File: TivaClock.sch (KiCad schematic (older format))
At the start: 6 parts

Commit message: add some more stuff
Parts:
- gave numbers to parts that had none: 4
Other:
- moved on the sheet: J2, J4, J?
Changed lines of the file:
@@
 $EndDescr
 $Comp
-L Conn_01x10 J?
+L Conn_01x10 J1
 U 1 1 5A5BEAC9
 P 2800 2300
-F 0 "J?" H 2800 2800 50  0000 C CNN
+F 0 "J1" H 2800 2800 50  0000 C CNN
 F 1 "Conn_01x10" H 2800 1700 50  0000 C CNN
 F 2 "" H 2800 2300 50  0001 C CNN
@@
 $EndComp
 $Comp
-L Conn_01x10 J?
+L Conn_01x10 J3
 U 1 1 5A5BEB8A
 P 3350 2300
-F 0 "J?" H 3350 2800 50  0000 C CNN
+F 0 "J3" H 3350 2800 50  0000 C CNN
 F 1 "Conn_01x10" H 3350 1700 50  0000 C CNN
 F 2 "" H 3350 2300 50  0001 C CNN
@@
 $EndComp
 $Comp
-L Conn_01x10 J?
+L Conn_01x10 J4
 U 1 1 5A5BED0F
-P 5600 2250
-F 0 "J?" H 5600 2750 50  0000 C CNN
-F 1 "Conn_01x10" H 5600 1650 50  0000 C CNN
-F 2 "" H 5600 2250 50  0001 C CNN
-F 3 "" H 5600 2250 50  0001 C CNN
-	1    5600 2250
+P 7800 2300
+F 0 "J4" H 7800 2800 50  0000 C CNN
+F 1 "Conn_01x10" H 7800 1700 50  0000 C CNN
+F 2 "" H 7800 2300 50  0001 C CNN
+F 3 "" H 7800 2300 50  0001 C CNN
+	1    7800 2300
 	1    0    0    -1
 $EndComp
 $Comp
-L Conn_01x10 J?
+L Conn_01x10 J2
 U 1 1 5A5BED3B
-P 6300 2300
-F 0 "J?" H 6300 2800 50  0000 C CNN
-F 1 "Conn_01x10" H 6300 1700 50  0000 C CNN
-F 2 "" H 6300 2300 50  0001 C CNN
-F 3 "" H 6300 2300 50  0001 C CNN
-	1    6300 2300
+P 8500 2300
+F 0 "J2" H 8500 2800 50  0000 C CNN
+F 1 "Conn_01x10" H 8500 1700 50  0000 C CNN
+F 2 "" H 8500 2300 50  0001 C CNN
+F 3 "" H 8500 2300 50  0001 C CNN
+	1    8500 2300
 	-1   0    0    -1
 $EndComp
@@
 L Conn_01x20 J?
 U 1 1 5A5BED71
-P 8200 4600
-F 0 "J?" H 8200 5600 50  0000 C CNN
-F 1 "Conn_01x20" H 8200 3500 50  0000 C CNN
-F 2 "" H 8200 4600 50  0001 C CNN
-F 3 "" H 8200 4600 50  0001 C CNN
-	1    8200 4600
+P 5200 4550
+F 0 "J?" H 5200 5550 50  0000 C CNN
+F 1 "Conn_01x20" H 5200 3450 50  0000 C CNN
+F 2 "" H 5200 4550 50  0001 C CNN
+F 3 "" H 5200 4550 50  0001 C CNN
+	1    5200 4550
 	1    0    0    -1
 $EndComp
@@
 L Conn_01x20 J?
 U 1 1 5A5BEDA4
-P 8950 4700
-F 0 "J?" H 8950 5700 50  0000 C CNN
-F 1 "Conn_01x20" H 8950 3600 50  0000 C CNN
-F 2 "" H 8950 4700 50  0001 C CNN
-F 3 "" H 8950 4700 50  0001 C CNN
-	1    8950 4700
+P 5950 4650
+F 0 "J?" H 5950 5650 50  0000 C CNN
+F 1 "Conn_01x20" H 5950 3550 50  0000 C CNN
+F 2 "" H 5950 4650 50  0001 C CNN
+F 3 "" H 5950 4650 50  0001 C CNN
+	1    5950 4650
 	-1   0    0    1
 $EndComp
-Text Label 7550 3700 0    60   ~ 0
+Text Label 4550 3650 0    60   ~ 0
 DS18B20
-Text Label 7550 3800 0    60   ~ 0
+Text Label 4550 3750 0    60   ~ 0
 1302RST
-Text Label 7550 3900 0    60   ~ 0
+Text Label 4550 3850 0    60   ~ 0
 1302IO
-Text Label 7550 4000 0    60   ~ 0
+Text Label 4550 3950 0    60   ~ 0
 1302CLK
-Text Label 7550 4100 0    60   ~ 0
+Text Label 4550 4050 0    60   ~ 0
 BEEP
-Text Label 7550 4500 0    60   ~ 0
+Text Label 4550 4450 0    60   ~ 0
 RESET
-Text Label 7550 4600 0    60   ~ 0
+Text Label 4550 4550 0    60   ~ 0
 RXD
-Text Label 7550 4700 0    60   ~ 0
+Text Label 4550 4650 0    60   ~ 0
 TXD
-Text Label 7550 4800 0    60   ~ 0
+Text Label 4550 4750 0    60   ~ 0
 MODE
-Text Label 7550 4900 0    60   ~ 0
+Text Label 4550 4850 0    60   ~ 0
 PLUS
-Text Label 7550 5000 0    60   ~ 0
+Text Label 4550 4950 0    60   ~ 0
 Bit8
-Text Label 7550 5100 0    60   ~ 0
+Text Label 4550 5050 0    60   ~ 0
 Bit9
-Text Label 7550 5200 0    60   ~ 0
+Text Label 4550 5150 0    60   ~ 0
 Bit10
-Text Label 7550 5300 0    60   ~ 0
+Text Label 4550 5250 0    60   ~ 0
 Bit11
-Text Label 7550 5600 0    60   ~ 0
+Text Label 4550 5550 0    60   ~ 0
 GND
-Text Label 9300 5600 0    60   ~ 0
+Text Label 6300 5550 0    60   ~ 0
 Bit0
-Text Label 9300 5500 0    60   ~ 0
+Text Label 6300 5450 0    60   ~ 0
 Bit1
-Text Label 9300 5400 0    60   ~ 0
+Text Label 6300 5350 0    60   ~ 0
 Bit2
-Text Label 9300 5300 0    60   ~ 0
+Text Label 6300 5250 0    60   ~ 0
 Bit3
-Text Label 9300 5200 0    60   ~ 0
+Text Label 6300 5150 0    60   ~ 0
 Bit4
-Text Label 9300 5100 0    60   ~ 0
+Text Label 6300 5050 0    60   ~ 0
 Bit5
-Text Label 9300 5000 0    60   ~ 0
+Text Label 6300 4950 0    60   ~ 0
 Bit6
-Text Label 9300 4900 0    60   ~ 0
+Text Label 6300 4850 0    60   ~ 0
 Bit7
-Text Label 9300 4600 0    60   ~ 0
+Text Label 6300 4550 0    60   ~ 0
 VCC
-Text Label 9300 4500 0    60   ~ 0
+Text Label 6300 4450 0    60   ~ 0
 X7
-Text Label 9300 4400 0    60   ~ 0
+Text Label 6300 4350 0    60   ~ 0
 X6
-Text Label 9300 4300 0    60   ~ 0
+Text Label 6300 4250 0    60   ~ 0
 X5
-Text Label 9300 4200 0    60   ~ 0
+Text Label 6300 4150 0    60   ~ 0
 X4
-Text Label 9300 4100 0    60   ~ 0
+Text Label 6300 4050 0    60   ~ 0
 X3
-Text Label 9300 4000 0    60   ~ 0
+Text Label 6300 3950 0    60   ~ 0
 X2
-Text Label 9300 3900 0    60   ~ 0
+Text Label 6300 3850 0    60   ~ 0
 X1
-Text Label 9300 3800 0    60   ~ 0
+Text Label 6300 3750 0    60   ~ 0
 X0
-Text Label 9300 3700 0    60   ~ 0
+Text Label 6300 3650 0    60   ~ 0
 VCC
 $EndSCHEMATC

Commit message: connect important peripherals
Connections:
- net BEEP: now also J2.2 (Pin_2), J?.5 (Pin_5)
- net GND: now also J2.1 (Pin_1), J3.2 (Pin_2), J?.20 (Pin_20)
- net RESET: now also J2.5 (Pin_5), J?.9 (Pin_9)
- net RXD: now also J1.3 (Pin_3), J?.10 (Pin_10)
- net TXD: now also J1.4 (Pin_4), J?.11 (Pin_11)
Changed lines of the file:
@@
 LIBS:contrib
 LIBS:valves
+LIBS:TivaClock-cache
 EELAYER 25 0
 EELAYER END
@@
 Text Label 6300 3650 0    60   ~ 0
 VCC
+Wire Wire Line
+	5000 4050 4350 4050
+Wire Wire Line
+	4350 4050 4350 3350
+Wire Wire Line
+	4350 3350 9000 3350
+Wire Wire Line
+	9000 3350 9000 2000
+Wire Wire Line
+	9000 2000 8700 2000
+Wire Wire Line
+	8700 2300 8900 2300
+Wire Wire Line
+	8900 2300 8900 3200
+Wire Wire Line
+	8900 3200 4200 3200
+Wire Wire Line
+	4200 3200 4200 4450
+Wire Wire Line
+	4200 4450 5000 4450
+Wire Wire Line
+	5000 4550 2150 4550
+Wire Wire Line
+	2150 4550 2150 2100
+Wire Wire Line
+	2150 2100 2600 2100
+Wire Wire Line
+	5000 4650 2300 4650
+Wire Wire Line
+	2300 4650 2300 2200
+Wire Wire Line
+	2300 2200 2600 2200
+Wire Wire Line
+	3550 2000 7000 2000
+Wire Wire Line
+	7000 2000 7000 1700
+Wire Wire Line
+	7000 1700 8800 1700
+Wire Wire Line
+	8800 1700 8800 1900
+Wire Wire Line
+	8800 1900 8700 1900
+Wire Wire Line
+	5000 5550 3900 5550
+Wire Wire Line
+	3900 5550 3900 2000
+Connection ~ 3900 2000
 $EndSCHEMATC

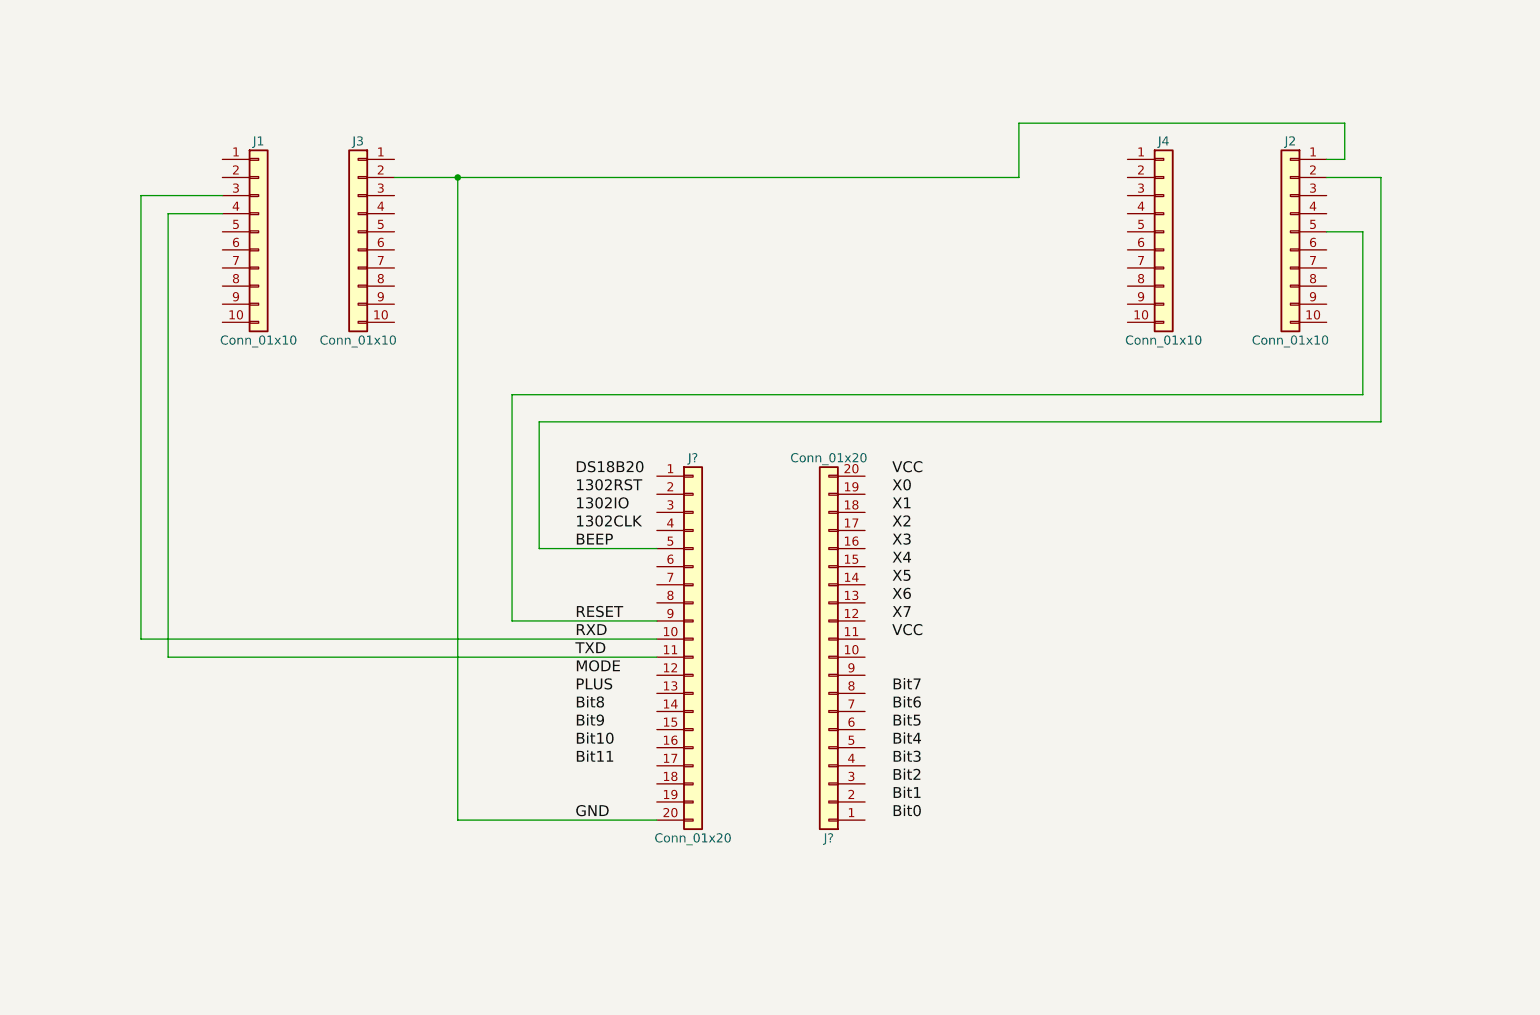
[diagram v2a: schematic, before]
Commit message: connected LED wires
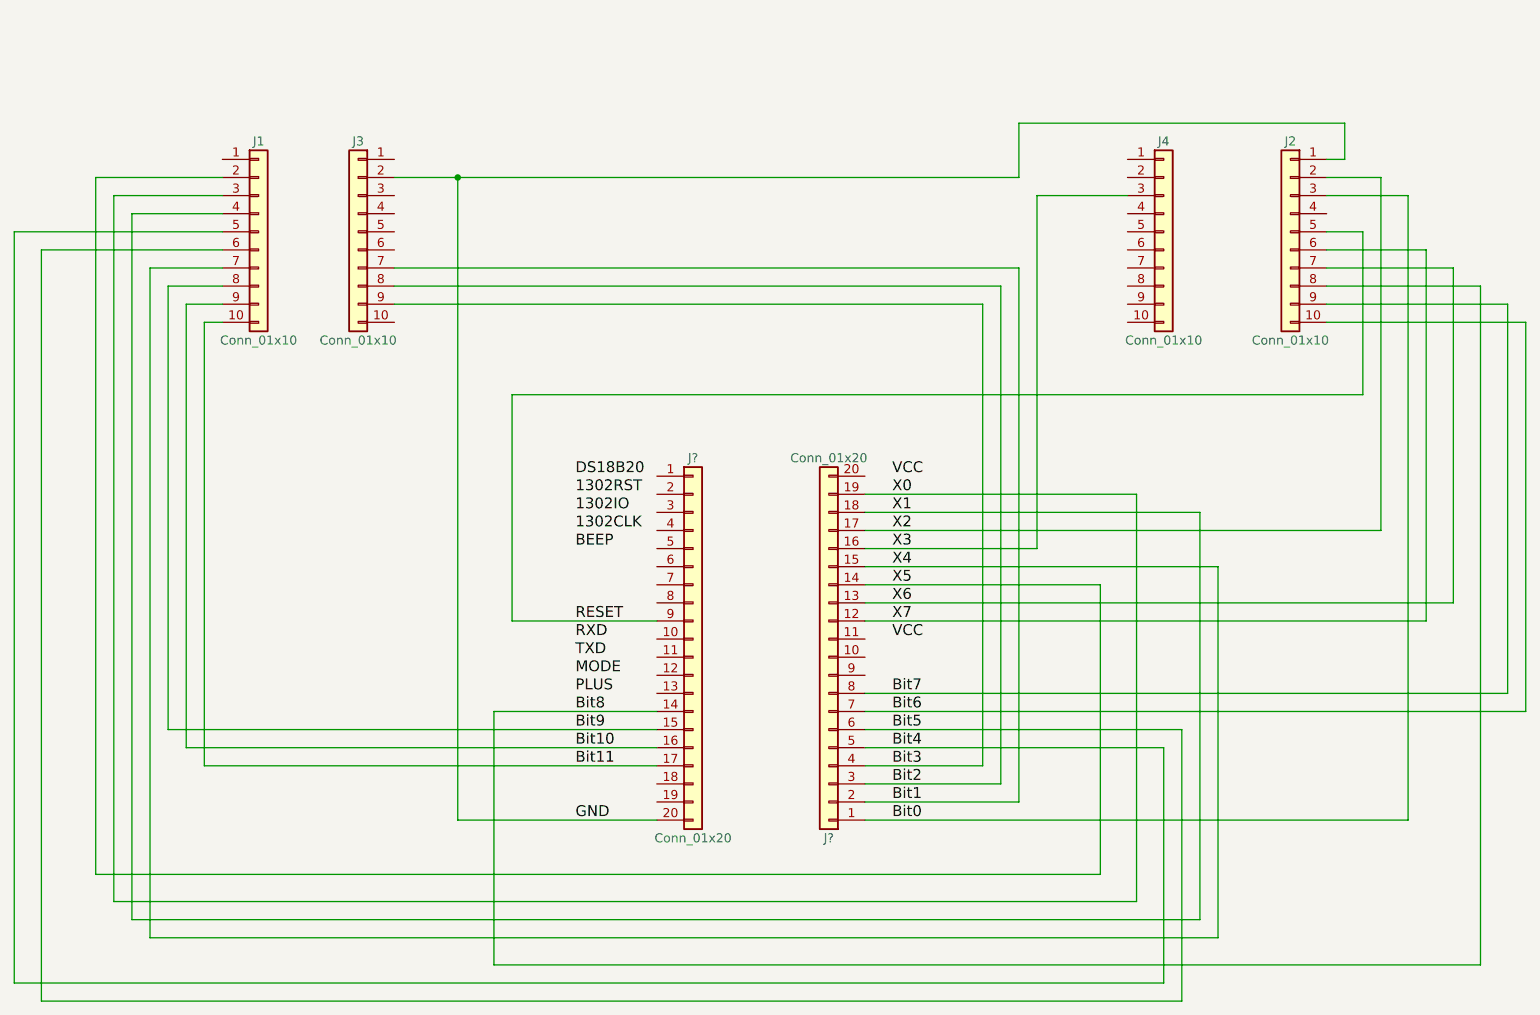
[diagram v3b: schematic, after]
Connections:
- net BEEP: no longer J2.2 (Pin_2), J?.5 (Pin_5)
- net Bit0: now also J2.3 (Pin_3), J?.1 (Pin_1)
- net Bit1: now also J3.7 (Pin_7), J?.2 (Pin_2)
- net Bit10: now also J1.9 (Pin_9), J?.16 (Pin_16)
- net Bit11: now also J1.10 (Pin_10), J?.17 (Pin_17)
- net Bit2: now also J3.8 (Pin_8), J?.3 (Pin_3)
- net Bit3: now also J3.9 (Pin_9), J?.4 (Pin_4)
- net Bit4: now also J1.5 (Pin_5), J?.5 (Pin_5)
- net Bit5: now also J1.6 (Pin_6), J?.6 (Pin_6)
- net Bit6: now also J2.10 (Pin_10), J?.7 (Pin_7)
- net Bit7: now also J2.9 (Pin_9), J?.8 (Pin_8)
- net Bit8: now also J2.8 (Pin_8), J?.14 (Pin_14)
- net Bit9: now also J1.8 (Pin_8), J?.15 (Pin_15)
- net RXD: no longer J1.3 (Pin_3), J?.10 (Pin_10)
- net TXD: no longer J1.4 (Pin_4), J?.11 (Pin_11)
- net X0: now also J1.3 (Pin_3), J?.19 (Pin_19)
- net X1: now also J1.4 (Pin_4), J?.18 (Pin_18)
- net X2: now also J2.2 (Pin_2), J?.17 (Pin_17)
- net X3: now also J4.3 (Pin_3), J?.16 (Pin_16)
- net X4: now also J1.7 (Pin_7), J?.15 (Pin_15)
- net X5: now also J1.2 (Pin_2), J?.14 (Pin_14)
- net X6: now also J2.7 (Pin_7), J?.13 (Pin_13)
- net X7: now also J2.6 (Pin_6), J?.12 (Pin_12)
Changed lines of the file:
@@
 VCC
-Wire Wire Line
-	5000 4050 4350 4050
-Wire Wire Line
-	4350 4050 4350 3350
-Wire Wire Line
-	4350 3350 9000 3350
-Wire Wire Line
-	9000 3350 9000 2000
-Wire Wire Line
-	9000 2000 8700 2000
 Wire Wire Line
 	8700 2300 8900 2300
@@
 	4200 4450 5000 4450
 Wire Wire Line
-	5000 4550 2150 4550
+	3550 2000 3900 2000
 Wire Wire Line
-	2150 4550 2150 2100
-Wire Wire Line
-	2150 2100 2600 2100
-Wire Wire Line
-	5000 4650 2300 4650
-Wire Wire Line
-	2300 4650 2300 2200
-Wire Wire Line
-	2300 2200 2600 2200
-Wire Wire Line
-	3550 2000 7000 2000
+	3900 2000 7000 2000
 Wire Wire Line
 	7000 2000 7000 1700
@@
 	3900 5550 3900 2000
 Connection ~ 3900 2000
+Wire Wire Line
+	2600 2000 1900 2000
+Wire Wire Line
+	1900 2000 1900 5850
+Wire Wire Line
+	1900 5850 7450 5850
+Wire Wire Line
+	7450 5850 7450 4250
+Wire Wire Line
+	7450 4250 6150 4250
+Wire Wire Line
+	2600 2100 2000 2100
+Wire Wire Line
+	2000 2100 2000 6000
+Wire Wire Line
+	2000 6000 7650 6000
+Wire Wire Line
+	7650 6000 7650 3750
+Wire Wire Line
+	7650 3750 6150 3750
+Wire Wire Line
+	2600 2200 2100 2200
+Wire Wire Line
+	2100 2200 2100 6100
+Wire Wire Line
+	2100 6100 8000 6100
+Wire Wire Line
+	8000 6100 8000 3850
+Wire Wire Line
+	8000 3850 6150 3850
+Wire Wire Line
+	2600 2500 2200 2500
+Wire Wire Line
+	2200 2500 2200 6200
+Wire Wire Line
+	2200 6200 8100 6200
+Wire Wire Line
+	8100 6200 8100 4150
+Wire Wire Line
+	8100 4150 6150 4150
+Wire Wire Line
+	2600 2600 2300 2600
+Wire Wire Line
+	2300 2600 2300 5050
+Wire Wire Line
+	2300 5050 5000 5050
+Wire Wire Line
+	2600 2700 2400 2700
+Wire Wire Line
+	2400 2700 2400 5150
+Wire Wire Line
+	2400 5150 5000 5150
+Wire Wire Line
+	2600 2800 2500 2800
+Wire Wire Line
+	2500 2800 2500 5250
+Wire Wire Line
+	2500 5250 5000 5250
+Wire Wire Line
+	8700 2000 9000 2000
+Wire Wire Line
+	9000 2000 9000 3950
+Wire Wire Line
+	9000 3950 6150 3950
+Wire Wire Line
+	8700 2100 9150 2100
+Wire Wire Line
+	9150 2100 9150 5550
+Wire Wire Line
+	9150 5550 6150 5550
+Wire Wire Line
+	8700 2400 9250 2400
+Wire Wire Line
+	9250 2400 9250 4450
+Wire Wire Line
+	9250 4450 6150 4450
+Wire Wire Line
+	8700 2500 9400 2500
+Wire Wire Line
+	9400 2500 9400 4350
+Wire Wire Line
+	9400 4350 6150 4350
+Wire Wire Line
+	8700 2600 9550 2600
+Wire Wire Line
+	9550 2600 9550 6350
+Wire Wire Line
+	9550 6350 4100 6350
+Wire Wire Line
+	4100 6350 4100 4950
+Wire Wire Line
+	4100 4950 5000 4950
+Wire Wire Line
+	8700 2700 9700 2700
+Wire Wire Line
+	9700 2700 9700 4850
+Wire Wire Line
+	9700 4850 6150 4850
+Wire Wire Line
+	8700 2800 9800 2800
+Wire Wire Line
+	9800 2800 9800 4950
+Wire Wire Line
+	9800 4950 6150 4950
+Wire Wire Line
+	3550 2500 7000 2500
+Wire Wire Line
+	7000 2500 7000 5450
+Wire Wire Line
+	7000 5450 6150 5450
+Wire Wire Line
+	3550 2600 6900 2600
+Wire Wire Line
+	6900 2600 6900 5350
+Wire Wire Line
+	6900 5350 6150 5350
+Wire Wire Line
+	3550 2700 6800 2700
+Wire Wire Line
+	6800 2700 6800 5250
+Wire Wire Line
+	6800 5250 6150 5250
+Wire Wire Line
+	7600 2100 7100 2100
+Wire Wire Line
+	7100 2100 7100 4050
+Wire Wire Line
+	7100 4050 6150 4050
+Wire Wire Line
+	2600 2300 1450 2300
+Wire Wire Line
+	1450 2300 1450 6450
+Wire Wire Line
+	1450 6450 7800 6450
+Wire Wire Line
+	7800 6450 7800 5150
+Wire Wire Line
+	7800 5150 6150 5150
+Wire Wire Line
+	2600 2400 1600 2400
+Wire Wire Line
+	1600 2400 1600 6550
+Wire Wire Line
+	1600 6550 7900 6550
+Wire Wire Line
+	7900 6550 7900 5050
+Wire Wire Line
+	7900 5050 6150 5050
 $EndSCHEMATC

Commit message: connected all remaining pins
except power
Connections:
- net 1302CLK: now also J4.5 (Pin_5), J?.4 (Pin_4)
- net 1302IO: now also J4.6 (Pin_6), J?.3 (Pin_3)
- net 1302RST: now also J4.7 (Pin_7), J?.2 (Pin_2)
- net BEEP: now also J4.4 (Pin_4), J?.5 (Pin_5)
- net DS18B20: now also J3.5 (Pin_5), J?.1 (Pin_1)
- net MODE: now also J4.10 (Pin_10), J?.12 (Pin_12)
- net PLUS: now also J2.4 (Pin_4), J?.13 (Pin_13)
- net RXD: now also J4.8 (Pin_8), J?.10 (Pin_10)
- net TXD: now also J4.9 (Pin_9), J?.11 (Pin_11)
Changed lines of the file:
@@
 	4200 4450 5000 4450
 Wire Wire Line
-	3550 2000 3900 2000
-Wire Wire Line
-	3900 2000 7000 2000
+	3550 2000 7000 2000
 Wire Wire Line
 	7000 2000 7000 1700
@@
 Wire Wire Line
 	7900 5050 6150 5050
+Wire Wire Line
+	7600 2200 4050 2200
+Wire Wire Line
+	4050 2200 4050 4050
+Wire Wire Line
+	4050 4050 5000 4050
+Wire Wire Line
+	7600 2800 3800 2800
+Wire Wire Line
+	3800 2800 3800 4750
+Wire Wire Line
+	3800 4750 5000 4750
+Wire Wire Line
+	8700 2200 8800 2200
+Wire Wire Line
+	8800 2200 8800 3400
+Wire Wire Line
+	8800 3400 3500 3400
+Wire Wire Line
+	3500 3400 3500 4850
+Wire Wire Line
+	3500 4850 5000 4850
+Wire Wire Line
+	7600 2300 4300 2300
+Wire Wire Line
+	4300 2300 4300 3950
+Wire Wire Line
+	4300 3950 5000 3950
+Wire Wire Line
+	4400 3850 5000 3850
+Wire Wire Line
+	4400 3850 4400 2400
+Wire Wire Line
+	4400 2400 7600 2400
+Wire Wire Line
+	7600 2500 7200 2500
+Wire Wire Line
+	7200 2500 7200 2950
+Wire Wire Line
+	7200 2950 4500 2950
+Wire Wire Line
+	4500 2950 4500 3750
+Wire Wire Line
+	4500 3750 5000 3750
+Wire Wire Line
+	3550 2300 3700 2300
+Wire Wire Line
+	3700 2300 3700 3650
+Wire Wire Line
+	3700 3650 5000 3650
+Wire Wire Line
+	7600 2600 7300 2600
+Wire Wire Line
+	7300 2600 7300 3050
+Wire Wire Line
+	7300 3050 3250 3050
+Wire Wire Line
+	3250 3050 3250 4550
+Wire Wire Line
+	3250 4550 5000 4550
+Wire Wire Line
+	7600 2700 7400 2700
+Wire Wire Line
+	7400 2700 7400 3100
+Wire Wire Line
+	7400 3100 3100 3100
+Wire Wire Line
+	3100 3100 3100 4650
+Wire Wire Line
+	3100 4650 5000 4650
 $EndSCHEMATC

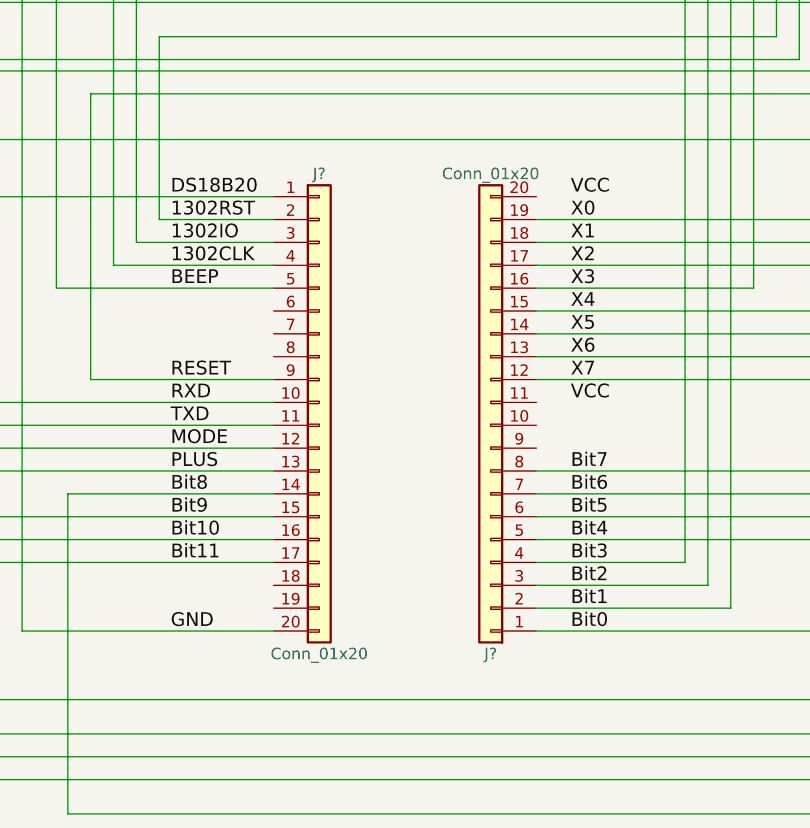
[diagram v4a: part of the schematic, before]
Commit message: annotate clock headers
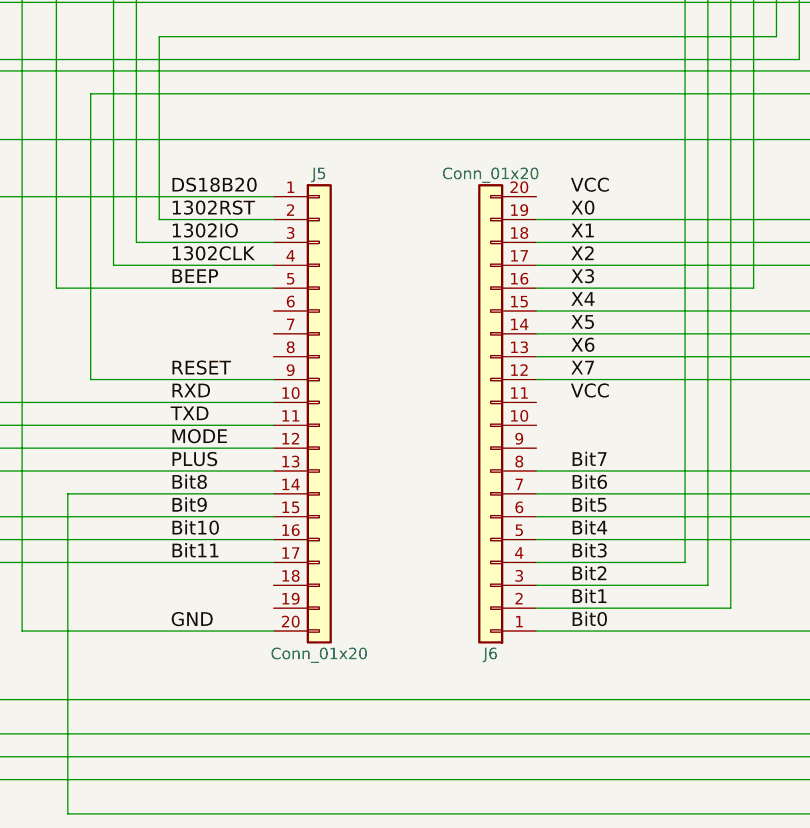
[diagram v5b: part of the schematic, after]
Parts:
- gave numbers to parts that had none: 2
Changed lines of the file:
@@
 $EndComp
 $Comp
-L Conn_01x20 J?
+L Conn_01x20 J5
 U 1 1 5A5BED71
 P 5200 4550
-F 0 "J?" H 5200 5550 50  0000 C CNN
+F 0 "J5" H 5200 5550 50  0000 C CNN
 F 1 "Conn_01x20" H 5200 3450 50  0000 C CNN
 F 2 "" H 5200 4550 50  0001 C CNN
@@
 $EndComp
 $Comp
-L Conn_01x20 J?
+L Conn_01x20 J6
 U 1 1 5A5BEDA4
 P 5950 4650
-F 0 "J?" H 5950 5650 50  0000 C CNN
+F 0 "J6" H 5950 5650 50  0000 C CNN
 F 1 "Conn_01x20" H 5950 3550 50  0000 C CNN
 F 2 "" H 5950 4650 50  0001 C CNN
